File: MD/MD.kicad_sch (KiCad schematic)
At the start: 36 parts, among them J1 Conn_01x05_Pin, J2 Conn_01x05_Pin, J3 Conn_02x07_Odd_Even, J4 Conn_01x06_Pin, Q1 2SA1015, SW1 SW_Push, SW2 SW_DIP_x04, SW3 SW_SPDT, SW4 SW_Push, U1 AZ1117-3.3, U2 MAX3485, U3 STM32C011F4Px, X1 MEMS_Oscillator_SiT2001B

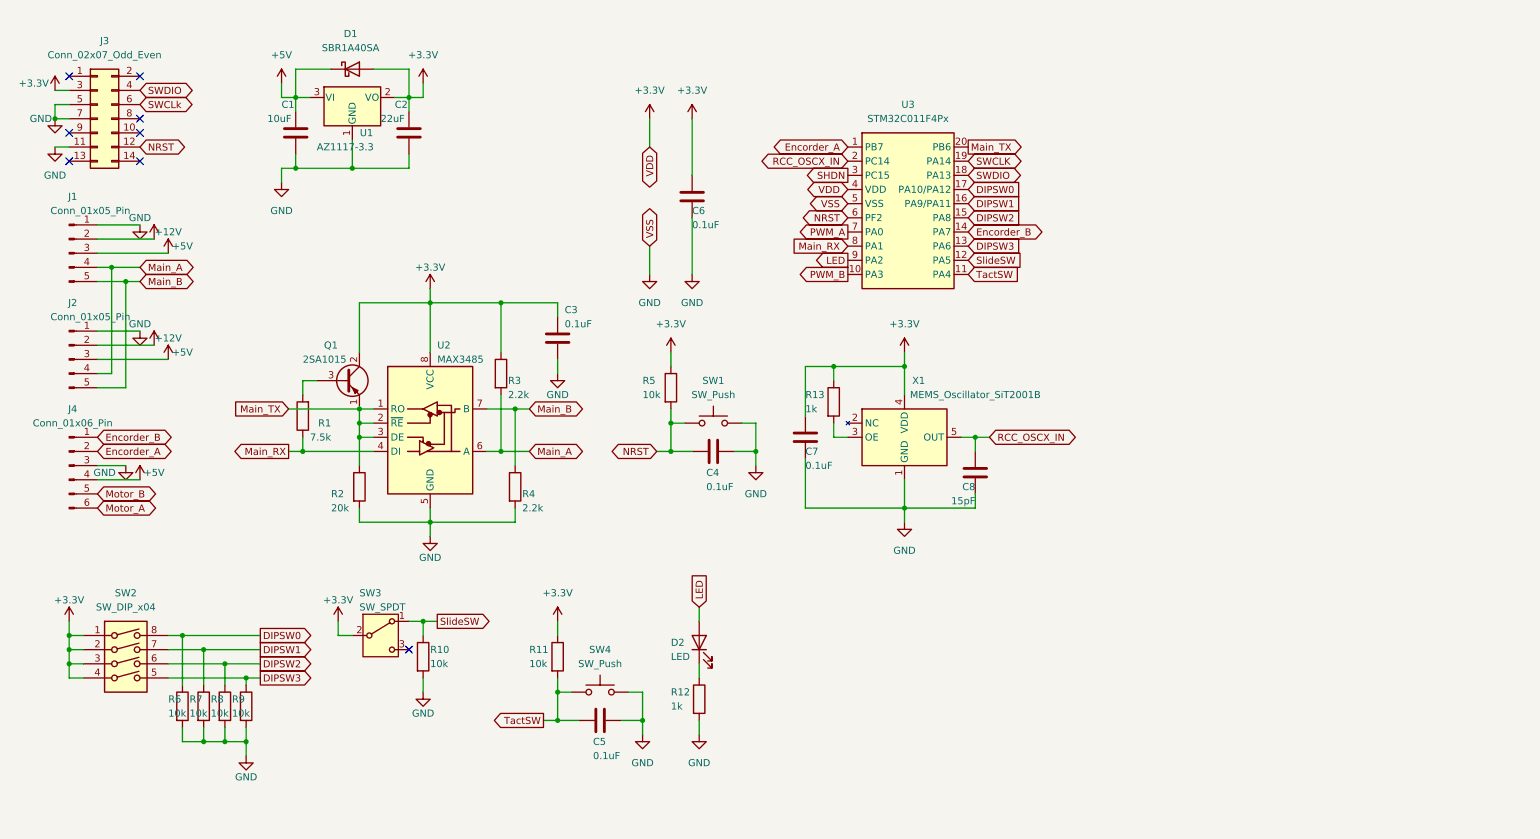
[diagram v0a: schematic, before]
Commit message: MD回路図完成
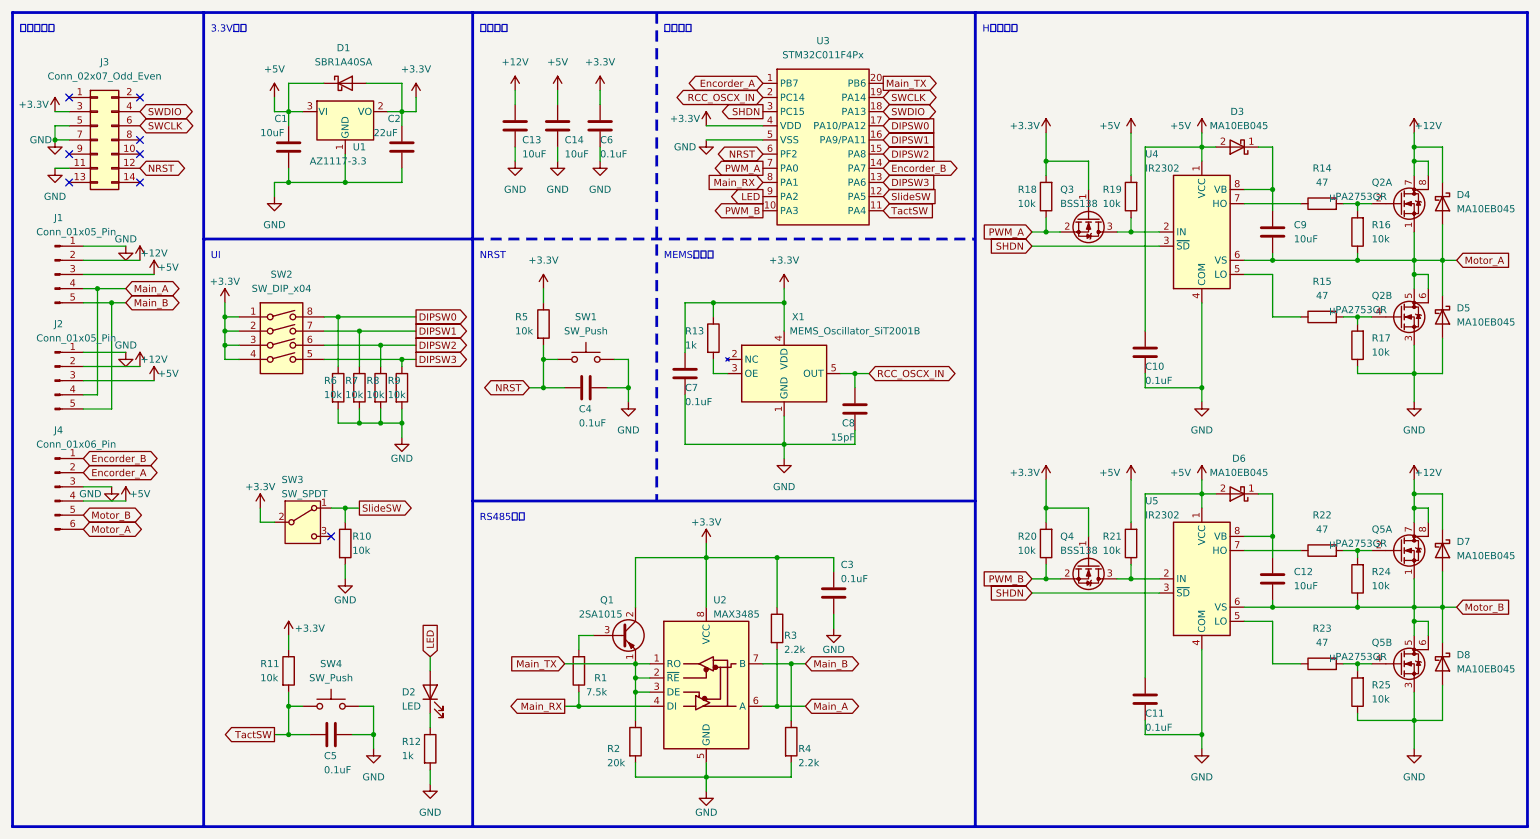
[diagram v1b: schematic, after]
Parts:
- added C10, C11: 0.1uF, Capacitor_SMD:C_0603_1608Metric_Pad1.08x0.95mm_HandSolder, symbol Device:C
- added C12, C13, C14, C9: 10uF, Capacitor_SMD:C_0603_1608Metric_Pad1.08x0.95mm_HandSolder, symbol Device:C
- added D3, D4, D5, D6, D7, D8: MA10EB045, Diode_SMD:Vishay_SMPA, symbol Device:D_Schottky
- added Q2, Q5: μPA2753GR, Package_SO:SOP-8_3.9x4.9mm_P1.27mm, symbol Device:Q_Dual_NMOS_S1G1S2G2D2D2D1D1
- added Q3, Q4: BSS138, Package_TO_SOT_SMD:SOT-23, symbol Transistor_FET:BSS138
- added R14, R15, R22, R23: 47, Resistor_SMD:R_0603_1608Metric_Pad0.98x0.95mm_HandSolder, symbol Device:R
- added R16, R17, R18, R19, R20, R21, R24, R25: 10k, Resistor_SMD:R_0603_1608Metric_Pad0.98x0.95mm_HandSolder, symbol Device:R
- added U4, U5: IR2302, IR2302:IR2302, symbol Driver_FET:IR2302
- J4: footprint (none) -> Connector_JST:JST_PH_B6B-PH-K_1x06_P2.00mm_Vertical
- U3: footprint (none) -> Package_SO:SSOP-20_4.4x6.5mm_P0.65mm
- X1: footprint (none) -> Package_TO_SOT_SMD:SOT-23-5_HandSoldering
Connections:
- net SWCLk is gone; now on net SWCLK: J3.6 (Pin_6)
- net +12V: now also C13.1, D4.1 (K), D7.1 (K), Q2.7 (D), Q2.8 (D), Q5.7 (D), Q5.8 (D)
- net +3.3V: now also Q3.1 (G), Q4.1 (G), R18.2, R20.2
- net +5V: now also C10.1, C11.1, C14.1, D3.2 (A), D6.2 (A), R19.2, R21.2, U4.1 (VCC), U5.1 (VCC)
- net GND: now also C10.2, C11.2, C13.2, C14.2, D5.2 (A), D8.2 (A), Q2.3 (S), Q5.3 (S), R17.1, R25.1, U4.4 (COM), U5.4 (COM)
- net Motor_A: now also C9.2, D4.2 (A), D5.1 (K), Q2.1 (S), Q2.5 (D), Q2.6 (D), R16.1, U4.6 (VS)
- net Motor_B: now also C12.2, D7.2 (A), D8.1 (K), Q5.1 (S), Q5.5 (D), Q5.6 (D), R24.1, U5.6 (VS)
- net PWM_A: now also Q3.2 (S), R18.1
- net PWM_B: now also Q4.2 (S), R20.1
- net SHDN: now also U4.3 (~{SD}), U5.3 (~{SD})
- new net: Q5.4 (G), R23.2, R25.2
- new net: Q4.3 (D), R21.1, U5.2 (IN)
- new net: R23.1, U5.5 (LO)
- new net: R22.1, U5.7 (HO)
- new net: C12.1, D6.1 (K), U5.8 (VB)
- new net: Q2.2 (G), R14.2, R16.2
- new net: Q3.3 (D), R19.1, U4.2 (IN)
- new net: R15.1, U4.5 (LO)
- new net: R14.1, U4.7 (HO)
- new net: C9.1, D3.1 (K), U4.8 (VB)
- new net: Q5.2 (G), R22.2, R24.2
- new net: Q2.4 (G), R15.2, R17.2
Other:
- note added: "3.3V生成"
- note added: "Hブリッジ"
- note added: "MEMS発振器"
- note added: "NRST"
- note added: "RS485変換"
- note added: "UI"
- note added: "コネクター"
- note added: "パスコン"
- note added: "マイコン"
- moved on the sheet: C1, C2, C3, C4, C5, C6, C7, C8, D1, D2, J1, J2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

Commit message: 細々修正 & PDF追加
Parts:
- removed SW4: SW_Push, Button_Switch_SMD:SW_Push_1P1T_NO_6x6mm_H9.5mm, symbol Switch:SW_Push
- added D10, D11, D12, D13, D9: LED, LED_SMD:LED_0603_1608Metric_Pad1.05x0.95mm_HandSolder, symbol Device:LED
- added R26: 2.2k, Resistor_SMD:R_0603_1608Metric_Pad0.98x0.95mm_HandSolder, symbol Device:R
- added R27: 1k, Resistor_SMD:R_0603_1608Metric_Pad0.98x0.95mm_HandSolder, symbol Device:R
- added R28: 1, Resistor_SMD:R_0603_1608Metric_Pad0.98x0.95mm_HandSolder, symbol Device:R
- added R29: 6.8k, Resistor_SMD:R_0603_1608Metric_Pad0.98x0.95mm_HandSolder, symbol Device:R
- added TP1: TestPoint, TestPoint:TestPoint_THTPad_D2.0mm_Drill1.0mm, symbol Connector:TestPoint
- D1: value SBR1A40SA -> MA10EB045; footprint Diode_SMD:D_SMA_Handsoldering -> Diode_SMD:Vishay_SMPA
- R11: value 10k -> 6.8k
- U4, U5: footprint IR2302:IR2302 -> Package_SO:SOP-8_3.76x4.96mm_P1.27mm
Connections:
- net +12V: now also D9.2 (A)
- net +3.3V: now also D11.2 (A); no longer R11.1
- net +5V: now also D10.2 (A)
- net GND: now also R11.2, R26.2, R27.2, TP1.1; no longer C5.1
- net Motor_A: now also R28.2, R29.1
- net Motor_B: now also C5.2, D12.1 (K), D13.2 (A)
- removed net TactSW: C5.2, R11.2, U3.11 (PA4)
- new net: C5.1, R28.1
- new net: D12.2 (A), D13.1 (K), R29.2
- new net: D10.1 (K), R26.1
- new net: D11.1 (K), R27.1
- new net: D9.1 (K), R11.1
- no-connect marks 8 -> 9
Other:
- note added: "スナバ回路"
- note added: "テストポイント"
- note added: "電源LED"
- moved on the sheet: C10, C11, C12, C9, D2, D3, D4, D5, D6, D7, D8, Q2A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

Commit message: 指摘された間違いを修正
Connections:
- net +3.3V: now also Q1.1 (E); no longer Q1.2 (C)
- net Main_TX: no longer Q1.1 (E), R2.1, U2.2 (~{RE}), U2.3 (DE)
- new net: Q1.2 (C), R2.1, U2.2 (~{RE}), U2.3 (DE)
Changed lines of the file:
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@@
   (junction (at 226.06 81.28) (diameter 0) (color 0 0 0 0)
-  )
-  (junction (at 124.46 129.54) (diameter 0) (color 0 0 0 0)
   )
   (junction (at 254 43.18) (diameter 0) (color 0 0 0 0)
@@
     (stroke (width 0) (type default))
   )
-  (wire (pts (xy 124.46 129.54) (xy 127 129.54))
+  (wire (pts (xy 111.76 129.54) (xy 127 129.54))
     (stroke (width 0) (type default))
   )
@@
   )
   (wire (pts (xy 269.24 22.86) (xy 264.16 22.86))
-    (stroke (width 0) (type default))
-  )
-  (wire (pts (xy 111.76 129.54) (xy 124.46 129.54))
     (stroke (width 0) (type default))
   )
@@
     )
   )
-  (symbol (lib_id "Transistor_BJT:2SA1015") (at 121.92 124.46 0) (unit 1)
-    (in_bom yes) (on_board yes) (dnp no)
-    (property "Reference" "Q1" (at 118.11 118.11 0)
-      (effects (font (size 1.27 1.27)) (justify left))
-    )
-    (property "Value" "2SA1015" (at 114.3 120.65 0)
-      (effects (font (size 1.27 1.27)) (justify left))
-    )
-    (property "Footprint" "Package_TO_SOT_THT:TO-92_Inline" (at 127 126.365 0)
+  (symbol (lib_id "Transistor_BJT:2SA1015") (at 121.92 124.46 0) (mirror x) (unit 1)
+    (in_bom yes) (on_board yes) (dnp no)
+    (property "Reference" "Q1" (at 118.11 130.81 0)
+      (effects (font (size 1.27 1.27)) (justify left))
+    )
+    (property "Value" "2SA1015" (at 114.3 128.27 0)
+      (effects (font (size 1.27 1.27)) (justify left))
+    )
+    (property "Footprint" "Package_TO_SOT_THT:TO-92_Inline" (at 127 122.555 0)
       (effects (font (size 1.27 1.27) italic) (justify left) hide)
     )

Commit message: 修正版回路図完成
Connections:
- net Main_RX: now also U2.1 (RO); no longer R1.1, U2.4 (DI)
- net Main_TX: now also R1.1, U2.4 (DI); no longer U2.1 (RO)
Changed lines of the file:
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@@
     (effects (font (size 1.27 1.27)) (justify left bottom))
   )
-  (global_label "Main_TX" (shape input) (at 111.76 129.54 180) (fields_autoplaced)
+  (global_label "Main_TX" (shape input) (at 111.76 137.16 180) (fields_autoplaced)
     (effects (font (size 1.27 1.27)) (justify right))
-    (property "Intersheetrefs" "${INTERSHEET_REFS}" (at 101.2759 129.54 0)
+    (property "Intersheetrefs" "${INTERSHEET_REFS}" (at 101.2759 137.16 0)
       (effects (font (size 1.27 1.27)) (justify right) hide)
     )
@@
     )
   )
-  (global_label "Main_RX" (shape output) (at 111.76 137.16 180) (fields_autoplaced)
+  (global_label "Main_RX" (shape output) (at 111.76 129.54 180) (fields_autoplaced)
     (effects (font (size 1.27 1.27)) (justify right))
-    (property "Intersheetrefs" "${INTERSHEET_REFS}" (at 100.9735 137.16 0)
+    (property "Intersheetrefs" "${INTERSHEET_REFS}" (at 100.9735 129.54 0)
       (effects (font (size 1.27 1.27)) (justify right) hide)
     )

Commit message: 回路図完成
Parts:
- removed C13, C14: 10uF, Capacitor_SMD:C_0603_1608Metric_Pad1.08x0.95mm_HandSolder, symbol Device:C
- removed D10, D11, D12, D13, D9: LED, LED_SMD:LED_0603_1608Metric_Pad1.05x0.95mm_HandSolder, symbol Device:LED
- removed D3, D4, D5: MA10EB045, Diode_SMD:Vishay_SMPA, symbol Device:D_Schottky
- removed J1: Conn_01x05_Pin, Connector_JST:JST_XH_B5B-XH-A_1x05_P2.50mm_Vertical, symbol Connector:Conn_01x05_Pin
- removed J3: Conn_02x07_Odd_Even, Tomoshibi_Library:BoxHeader_2x07_P1.27mm_Horizontal, symbol Connector_Generic:Conn_02x07_Odd_Even
- removed Q3, Q4: BSS138, Package_TO_SOT_SMD:SOT-23, symbol Transistor_FET:BSS138
- removed Q5: μPA2753GR, Package_SO:SOP-8_3.9x4.9mm_P1.27mm, symbol Device:Q_Dual_NMOS_S1G1S2G2D2D2D1D1
- removed R23: 47, Resistor_SMD:R_0603_1608Metric_Pad0.98x0.95mm_HandSolder, symbol Device:R
- removed R24, R25: 10k, Resistor_SMD:R_0603_1608Metric_Pad0.98x0.95mm_HandSolder, symbol Device:R
- removed R26: 2.2k, Resistor_SMD:R_0603_1608Metric_Pad0.98x0.95mm_HandSolder, symbol Device:R
- removed R27: 1k, Resistor_SMD:R_0603_1608Metric_Pad0.98x0.95mm_HandSolder, symbol Device:R
- removed R28: 1, Resistor_SMD:R_0603_1608Metric_Pad0.98x0.95mm_HandSolder, symbol Device:R
- removed R29: 6.8k, Resistor_SMD:R_0603_1608Metric_Pad0.98x0.95mm_HandSolder, symbol Device:R
- removed U1: AZ1117-3.3, Package_TO_SOT_SMD:SOT-223-3_TabPin2, symbol Regulator_Linear:AZ1117-3.3
- removed U2: MAX3485, Package_SO:SOP-8_3.76x4.96mm_P1.27mm, symbol Interface_UART:MAX3485
- removed U3: STM32C011F4Px, Package_SO:SSOP-20_4.4x6.5mm_P0.65mm, symbol Tomoshibi_Library:STM32C011F4Px
- added D10, D11, D9: CUS01, Diode_SMD:D_SOD-323_HandSoldering, symbol Device:D_Schottky
- added D3, D4: OSR50603C1E, LED_SMD:LED_0603_1608Metric_Pad1.05x0.95mm_HandSolder, symbol Device:LED
- added D5: OSBL1608C1A, LED_SMD:LED_0603_1608Metric_Pad1.05x0.95mm_HandSolder, symbol Device:LED
- added J1: Conn_02x07_Odd_Even, Tomoshibi_Library:BoxHeader_2x07_P1.27mm_Horizontal, symbol Connector_Generic:Conn_02x07_Odd_Even
- added J3: Conn_01x05_Pin, Connector_JST:JST_XH_B5B-XH-A_1x05_P2.50mm_Vertical, symbol Connector:Conn_01x05_Pin
- added Q3: μPA2753GR, Package_SO:SOP-8_3.9x4.9mm_P1.27mm, symbol Device:Q_Dual_NMOS_S1G1S2G2D2D2D1D1
- added U1: RT9080-33GJ5, Package_TO_SOT_SMD:TSOT-23-5, symbol Tomoshibi_Library:RT9080-33GJ5
- added U2: STM32C011F4Px, Package_SO:TSSOP-20_4.4x6.5mm_P0.65mm, symbol Tomoshibi_Library:STM32C011F4Px
- added U3: MAX3485, Package_SO:SOP-8_3.76x4.96mm_P1.27mm, symbol Interface_UART:MAX3485
- C1: value 10uF -> 1uF
- C10, C3, C4: value 0.1uF -> 10uF
- C2: value 22uF -> 1uF; footprint Capacitor_SMD:C_0805_2012Metric_Pad1.18x1.45mm_HandSolder -> Capacitor_SMD:C_0603_1608Metric_Pad1.08x0.95mm_HandSolder
- C8: value 15pF -> 0.1uF
- C9: value 10uF -> 0.1uF
- D1, D6, D7, D8: value MA10EB045 -> CUS01; footprint Diode_SMD:Vishay_SMPA -> Diode_SMD:D_SOD-323_HandSoldering
- D2: value LED -> OSR50603C1E
- Q1: value 2SA1015 -> 2SA1037AK; footprint Package_TO_SOT_THT:TO-92_Inline -> Package_TO_SOT_SMD:SOT-23-3
- R1: value 7.5k -> 1k
- R11: value 6.8k -> 10k
- R12, R13: value 1k -> 10k
- R14: value 47 -> 1k
- R15: value 47 -> 100
- R16, R17, R18: value 10k -> 100
- R2: value 20k -> 6.8k
- R22: value 47 -> 10k
- R4: value 2.2k -> 1k
- R5: value 10k -> 7.5k
- R6: value 10k -> 20k
- R7, R8: value 10k -> 2.2k
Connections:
- net Main_TX is gone; now on net +3.3V: R1.1
- net +12V: now also C11.1, C3.1, C9.1, D2.2 (A), D6.2 (A), U4.1 (VCC), U5.1 (VCC), D10.1 (K), D9.2 (A), J3.2 (Pin_2), Q3.7 (D), Q3.8 (D)
- net +3.3V: now also C5.1, R7.1, D4.2 (A), J1.3 (Pin_3), U2.4 (VDD), U3.8 (VCC); no longer C2.1, C3.1, D1.2 (A), R13.1, R18.2, R20.2, R3.1, R5.1
- net +5V: now also C4.1, D3.2 (A), J3.3 (Pin_3), U1.1 (VIN), U1.3 (EN); no longer C10.1, C11.1, D6.2 (A), R19.2, R21.2, U4.1 (VCC), U5.1 (VCC)
- net DIPSW0: now also R9.1, U2.17 (PA10/PA12); no longer R6.1
- net DIPSW1: now also R10.1, U2.16 (PA9/PA11); no longer R7.1
- net DIPSW2: now also R11.1, U2.15 (PA8); no longer R8.1
- net DIPSW3: now also R12.1, U2.13 (PA6); no longer R9.1
- net Encorder_A: now also U2.1 (PB7)
- net Encorder_B: now also U2.14 (PA7)
- net GND: now also C4.2, C5.2, C9.2, R13.2, R14.2, R20.1, R22.1, R3.2, X1.5 (OUT), D11.2 (A), J1.11 (Pin_11), J1.5 (Pin_5), J1.7 (Pin_7), J3.1 (Pin_1), Q3.3 (S), U1.2 (GND), U1.4 (NC), U2.2 (PC14), U2.5 (VSS), U3.5 (GND); no longer C10.2, C4.1, R17.1, R7.2
- net LED: now also D5.2 (A), U2.9 (PA2); no longer D2.2 (A)
- net Main_A: now also J3.4 (Pin_4); no longer R3.2
- net Main_B: now also J3.5 (Pin_5); no longer R4.1
- net Motor_A: now also C10.2, D7.2 (A), D8.1 (K), R19.1, Q3.1 (S), Q3.5 (D), Q3.6 (D); no longer C9.2, Q2.1 (S), Q2.5 (D), Q2.6 (D), R16.1
- net Motor_B: now also Q2.1 (S), Q2.5 (D), Q2.6 (D), R21.1, D10.2 (A), D11.1 (K); no longer C5.2, D7.2 (A), D8.1 (K)
- net NRST: now also C8.2, J1.12 (Pin_12), U2.6 (PF2); no longer C4.2, R5.2
- net PWM_A: now also U4.2 (IN), U2.7 (PA0); no longer R18.1
- net PWM_B: now also U5.2 (IN), U2.10 (PA3); no longer R20.1
- net SHDN: now also U2.3 (PC15)
- net SWCLK: now also J1.6 (Pin_6), U2.19 (PA14)
- net SWDIO: now also J1.4 (Pin_4), U2.18 (PA13)
- net SlideSW: now also R13.1, U2.12 (PA5); no longer R10.1
- net at X1.3 (OE): now also R1.2; no longer R13.2
- net at U5.5 (LO): now also R16.1
- net at U5.7 (HO): now also R15.1; no longer R22.1
- net at C12.1, U5.8 (VB): now also D9.1 (K); no longer D6.1 (K)
- net at Q1.3 (B): now also R5.2; no longer R1.2
- net at U4.5 (LO): now also R18.1; no longer R15.1
- net at R14.1: now also D5.1 (K); no longer U4.7 (HO)
- net at U4.8 (VB): now also C10.1, D6.1 (K); no longer C9.1
- net at R2.1: now also D2.1 (K); no longer Q1.2 (C)
- net at R22.2: now also Q2.4 (G), R16.2
- removed net RCC_OSCX_IN: C8.2, X1.5 (OUT)
- new net: D4.1 (K), R4.1
- new net: R17.1, U4.7 (HO)
- new net: Q3.2 (G), R17.2, R19.2
- new net: D3.1 (K), R3.1
- new net: Q3.4 (G), R18.2, R20.2
- new net: Q2.2 (G), R15.2, R21.2
- new net +3V3: C2.1, D1.2 (A), U1.5 (VOUT)
- new net MD_A: R7.2, U3.6 (A)
- new net MD_B: R8.1, U3.7 (B)
- new net MD_RX/MAIN_TX: Q1.2 (C), R6.1, U2.8 (PA1), U3.1 (RO), U3.2 (~{RE}), U3.3 (DE)
- new net MD_TX/MAIN_RX: R5.1, U2.20 (PB6), U3.4 (DI)
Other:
- note added: "C011"
- note added: "RS485"
- note added: "コネクタ"
- note added: "電源LED・テストポイント"
- note removed: "RS485変換"
- note removed: "コネクター"
- note removed: "スナバ回路"
- note removed: "テストポイント"
- note removed: "マイコン"
- note removed: "電源LED"
